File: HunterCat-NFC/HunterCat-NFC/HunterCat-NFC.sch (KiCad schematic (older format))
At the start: 66 parts, among them J1 Battery, J2 Conn_01x06_Female, P1 USB_C_Plug_USB2.0, Q1 DMG3415U-7, SW1 RESET, U1 ATSAMD21E18A, U2 PN7150B0HN_C11002E-PN7150B0HN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, U3 MCP73831-3-OT, U4 AP2112K-3.3, U5 GD25Q16CEIGR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

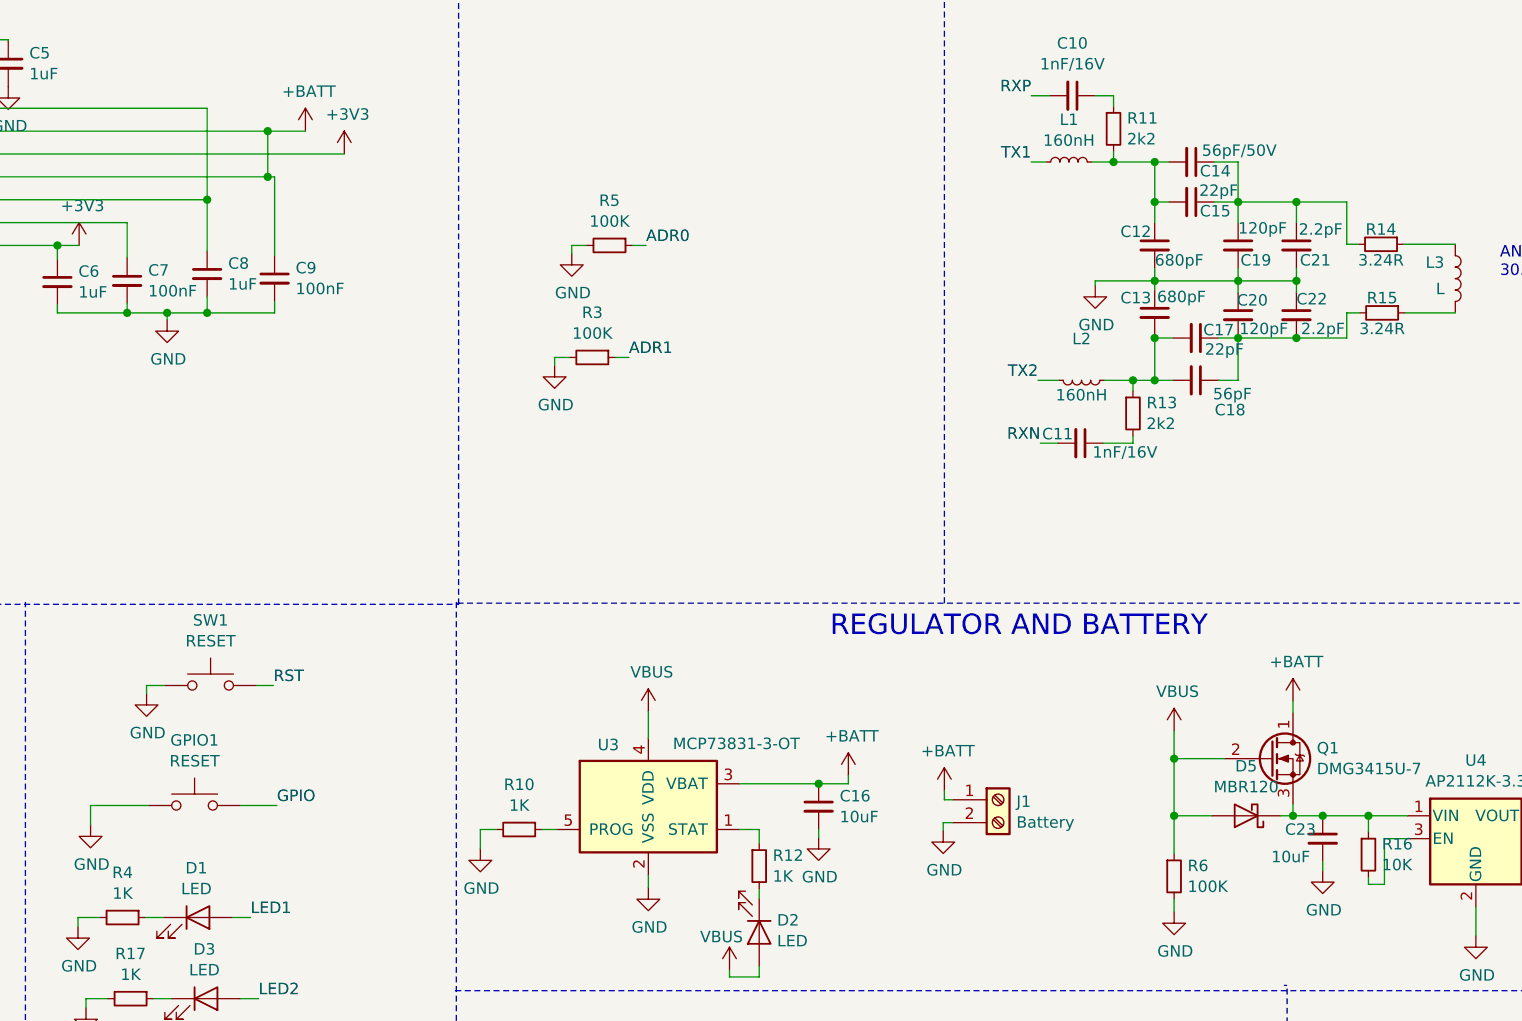
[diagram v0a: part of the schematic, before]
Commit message: modify Rf frontend
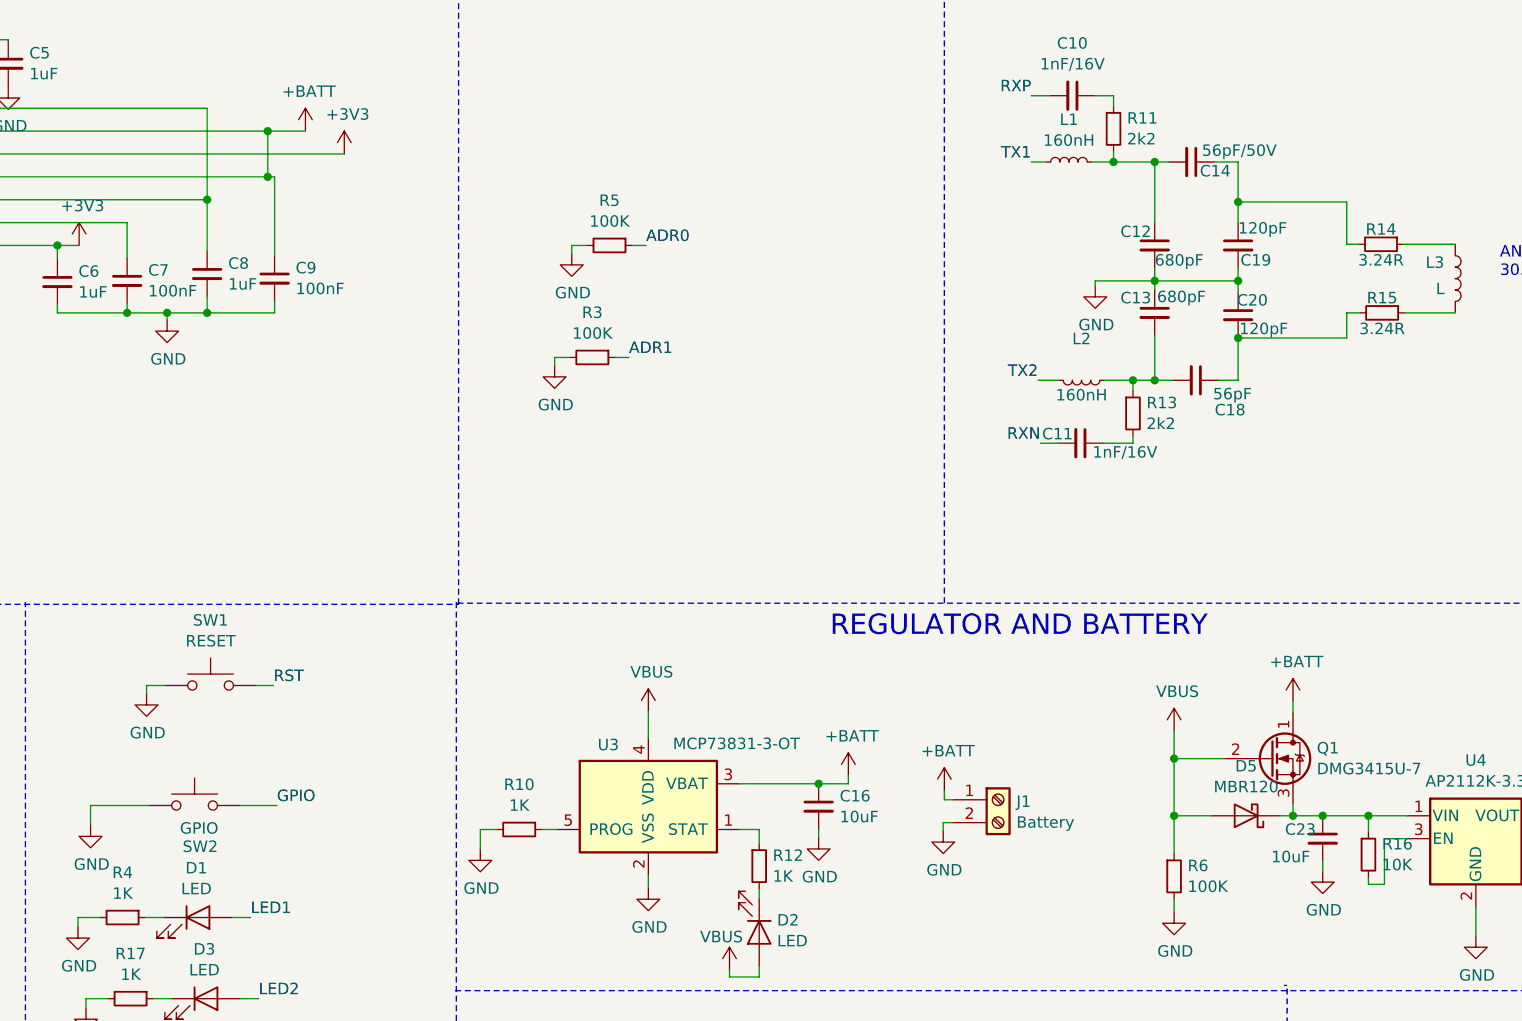
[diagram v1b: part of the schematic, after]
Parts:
- removed C15, C17: 22pF, Capacitor_SMD:C_0603_1608Metric_Pad1.05x0.95mm_HandSolder, symbol Device:C_Small
- removed C21, C22: 2.2pF, Capacitor_SMD:C_0603_1608Metric_Pad1.05x0.95mm_HandSolder, symbol Device:C_Small
- SW2: renamed from GPIO1; value RESET -> GPIO
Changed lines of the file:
@@
-$EndComp
-$Comp
-L Device:C_Small C15
-U 1 1 5E463B1E
-P 8930 1650
-F 0 "C15" V 8970 1755 50  0000 C CNN
-F 1 "22pF" V 8880 1770 50  0000 C CNN
-F 2 "Capacitor_SMD:C_0603_1608Metric_Pad1.05x0.95mm_HandSolder" H 8930 1650 50  0001 C CNN
-F 3 "~" H 8930 1650 50  0001 C CNN
-F 4 "06035A220JAT4A" H 8930 1650 50  0001 C CNN "manf#"
-	1    8930 1650
-	0    1    1    0
 $EndComp
 $Comp
@@
 $EndComp
 $Comp
-L Device:C_Small C21
-U 1 1 5E4643F2
-P 9390 1840
-F 0 "C21" H 9405 1775 50  0000 L CNN
-F 1 "2.2pF" H 9400 1910 50  0000 L CNN
-F 2 "Capacitor_SMD:C_0603_1608Metric_Pad1.05x0.95mm_HandSolder" H 9390 1840 50  0001 C CNN
-F 3 "~" H 9390 1840 50  0001 C CNN
-F 4 "GCM0335C1E2R2CA16D" H 9390 1840 50  0001 C CNN "manf#"
-	1    9390 1840
-	1    0    0    -1
-$EndComp
-$Comp
 L Device:C_Small C13
 U 1 1 5E464863
@@
 	1    9135 2145
 	1    0    0    -1
-$EndComp
-$Comp
-L Device:C_Small C22
-U 1 1 5E464CCF
-P 9390 2145
-F 0 "C22" H 9390 2215 50  0000 L CNN
-F 1 "2.2pF" H 9410 2085 50  0000 L CNN
-F 2 "Capacitor_SMD:C_0603_1608Metric_Pad1.05x0.95mm_HandSolder" H 9390 2145 50  0001 C CNN
-F 3 "~" H 9390 2145 50  0001 C CNN
-F 4 "GCM0335C1E2R2CA16D" H 9390 2145 50  0001 C CNN "manf#"
-	1    9390 2145
-	1    0    0    -1
-$EndComp
-$Comp
-L Device:C_Small C17
-U 1 1 5E4654A1
-P 8950 2245
-F 0 "C17" V 8915 2345 50  0000 C CNN
-F 1 "22pF" V 9000 2370 50  0000 C CNN
-F 2 "Capacitor_SMD:C_0603_1608Metric_Pad1.05x0.95mm_HandSolder" H 8950 2245 50  0001 C CNN
-F 3 "~" H 8950 2245 50  0001 C CNN
-F 4 "06035A220JAT4A" H 8950 2245 50  0001 C CNN "manf#"
-	1    8950 2245
-	0    1    1    0
 $EndComp
 $Comp
@@
 	8590 1475 8770 1475
 Connection ~ 8590 1475
-Wire Wire Line
-	8830 1650 8770 1650
-Wire Wire Line
-	8770 1650 8770 1475
 Connection ~ 8770 1475
 Wire Wire Line
@@
 	9030 1475 9135 1475
 Wire Wire Line
-	9135 1650 9030 1650
-Wire Wire Line
-	8770 1650 8770 1740
-Connection ~ 8770 1650
-Wire Wire Line
 	8770 1940 8770 1995
 Wire Wire Line
 	9135 2045 9135 1995
-Wire Wire Line
-	9390 1940 9390 1995
-Wire Wire Line
-	9390 1995 9135 1995
-Connection ~ 9390 1995
-Wire Wire Line
-	9390 1995 9390 2045
 Connection ~ 9135 1995
 Wire Wire Line
@@
 	8770 1995 8770 2035
 Wire Wire Line
-	9135 2245 9050 2245
-Wire Wire Line
-	8850 2245 8770 2245
-Wire Wire Line
-	8770 2245 8770 2235
-Wire Wire Line
 	9050 2430 9135 2430
 Wire Wire Line
@@
 	8850 2430 8770 2430
 Wire Wire Line
-	8770 2430 8770 2245
-Connection ~ 8770 2245
-Wire Wire Line
 	8770 2430 8675 2430
 Connection ~ 8770 2430
@@
 Wire Wire Line
 	8675 2705 8545 2705
-Wire Wire Line
-	9390 2245 9135 2245
 Wire Wire Line
 	8770 1995 8510 1995
@@
 Wire Wire Line
 	9610 2135 9610 2245
-Wire Wire Line
-	9610 2245 9390 2245
-Connection ~ 9390 2245
 Text Label 8230 1185 2    50   ~ 0
 RXP
@@
 $EndComp
 Wire Wire Line
-	9390 1740 9390 1650
-Wire Wire Line
-	9390 1650 9610 1650
-Wire Wire Line
 	9135 1475 9135 1650
-Wire Wire Line
-	9135 1650 9390 1650
 Connection ~ 9135 1650
 Wire Wire Line
 	9135 1650 9135 1740
-Connection ~ 9390 1650
 $Comp
 L Device:C_Small C25
@@
 	8505 5870 8505 5955
 $Comp
-L Switch:SW_Push GPIO1
+L Switch:SW_Push SW2
 U 1 1 5F214F20
 P 4570 4290
-F 0 "GPIO1" H 4570 4575 50  0000 C CNN
-F 1 "RESET" H 4570 4484 50  0000 C CNN
+F 0 "SW2" H 4595 4110 50  0000 C CNN
+F 1 "GPIO" H 4590 4190 50  0000 C CNN
 F 2 "Button_Switch_SMD:SW_SPST_TL3342" H 4570 4490 50  0001 C CNN
 F 3 "~" H 4570 4490 50  0001 C CNN
@@
 Wire Wire Line
 	3460 3140 3500 3140
+Wire Wire Line
+	8770 1475 8770 1740
+Wire Wire Line
+	8770 2235 8770 2430
+Wire Wire Line
+	9135 2245 9610 2245
+Wire Wire Line
+	9135 1650 9610 1650
 $EndSCHEMATC

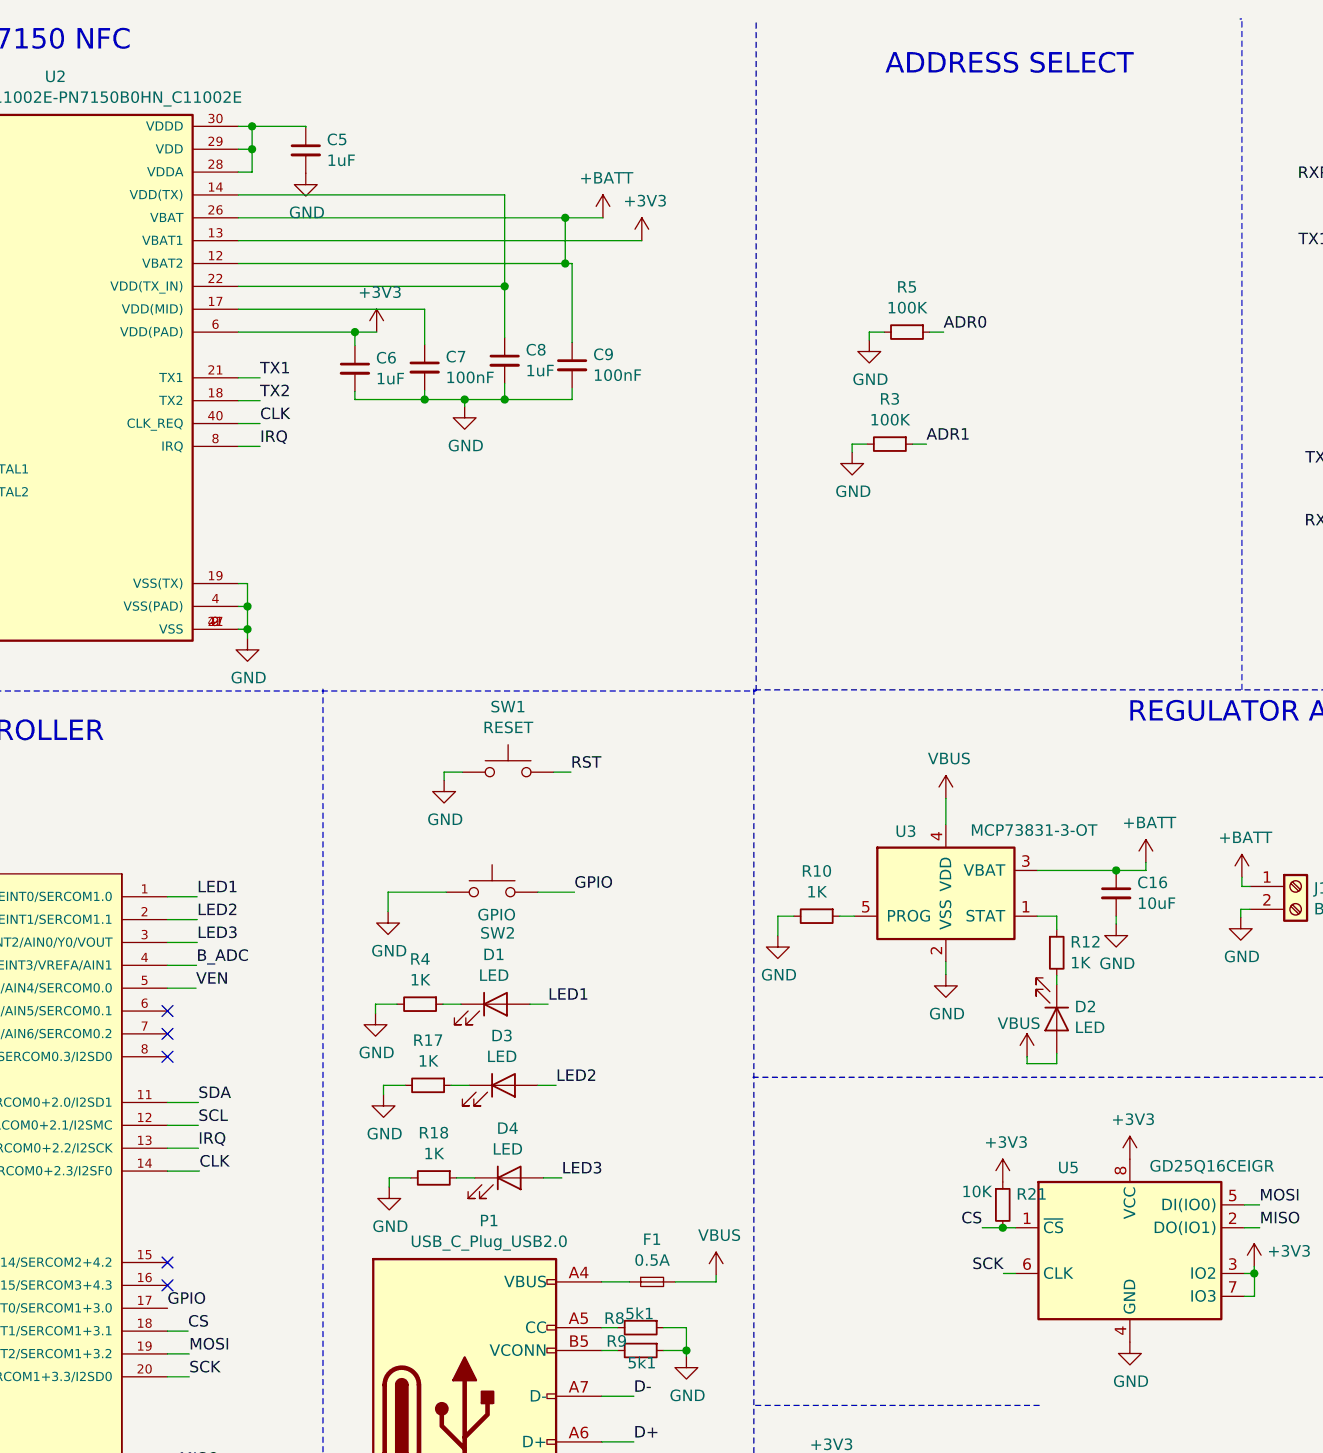
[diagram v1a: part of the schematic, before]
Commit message: Add button
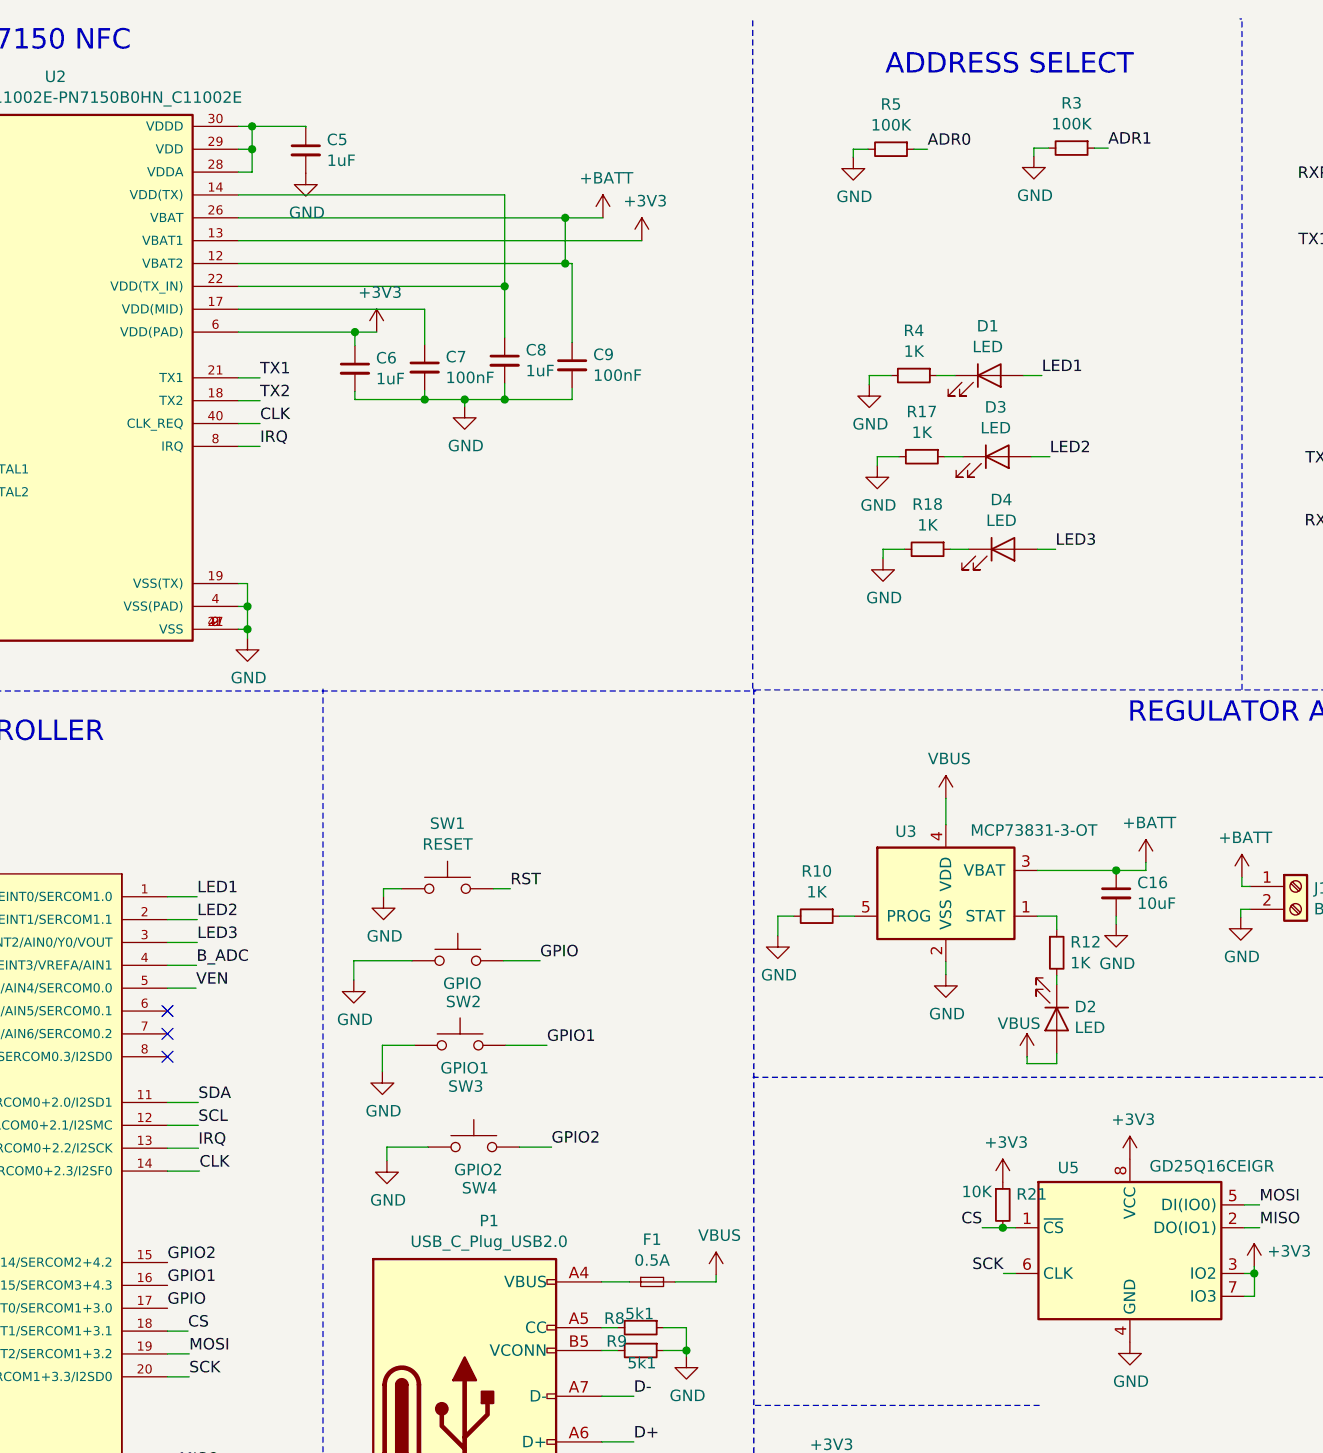
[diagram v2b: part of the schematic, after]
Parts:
- added SW3: GPIO1, Button_Switch_SMD:SW_SPST_TL3342, symbol Switch:SW_Push
- added SW4: GPIO2, Button_Switch_SMD:SW_SPST_TL3342, symbol Switch:SW_Push
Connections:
- net GND: now also SW3.1, SW4.1
- net GPIO2: now reaches U1.15 (PA14/EINT14/SERCOM2+4.2)
- net GPIO2: now also SW4.2
- net GPIO1: now reaches U1.16 (PA15/EINT15/SERCOM3+4.3)
- net GPIO1: now also SW3.2
- no-connect marks 10 -> 8
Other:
- moved on the sheet: D1, D3, D4, R17, R18, R3, R4, R5, SW1, SW2

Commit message: update to 1.0v
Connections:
- net CLK: now also U1.17 (PA16/I2C/EINT0/SERCOM1+3.0); no longer U1.14 (PA11/EINT11/AIN19/SERCOM0+2.3/I2SF0)
- net GPIO: now also SW4.2, U1.25 (PA27/EINT15); no longer SW2.2, U1.17 (PA16/I2C/EINT0/SERCOM1+3.0)
- net GPIO1: now also SW2.2, U1.14 (PA11/EINT11/AIN19/SERCOM0+2.3/I2SF0); no longer SW3.2, U1.16 (PA15/EINT15/SERCOM3+4.3)
- net GPIO2: now also SW3.2, U1.13 (PA10/EINT10/AIN18/SERCOM0+2.2/I2SCK); no longer SW4.2, U1.15 (PA14/EINT14/SERCOM2+4.2)
- net IRQ: now also U1.16 (PA15/EINT15/SERCOM3+4.3); no longer U1.13 (PA10/EINT10/AIN18/SERCOM0+2.2/I2SCK)
- net VEN: now also U1.15 (PA14/EINT14/SERCOM2+4.2); no longer U1.5 (PA04/EINT4/VREFB/AIN4/SERCOM0.0)
- no-connect marks 8 -> 7
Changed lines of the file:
@@
 Wire Wire Line
 	3150 5510 3290 5510
-Text Label 3285 5410 0    50   ~ 0
-IRQ
-Text Label 3290 5510 0    50   ~ 0
-CLK
 $Comp
 L Switch:SW_Push SW1
@@
 NoConn ~ 3150 5010
 NoConn ~ 3150 7310
-NoConn ~ 3150 7210
 NoConn ~ 3150 6910
 Text Notes 7350 3560 0    89   ~ 0
@@
 Wire Wire Line
 	3150 4710 3275 4710
-Text Label 3275 4710 0    50   ~ 0
+Text Label 3150 5910 0    50   ~ 0
 VEN
 Wire Wire Line
@@
 Wire Wire Line
 	8505 5870 8505 5955
-Text Label 3150 6110 0    50   ~ 0
+Text Label 3255 7210 0    50   ~ 0
 GPIO
 $Comp
@@
 Wire Wire Line
 	9135 1650 9610 1650
-Text Label 3150 5910 0    50   ~ 0
+Text Label 3285 5410 0    50   ~ 0
 GPIO2
-Text Label 3150 6010 0    50   ~ 0
+Text Label 3290 5510 0    50   ~ 0
 GPIO1
 Wire Wire Line
@@
 Wire Wire Line
 	4690 5405 4830 5405
-Text Label 4830 5405 0    50   ~ 0
+Text Label 4810 4960 0    50   ~ 0
 GPIO2
 $Comp
@@
 	1    0    0    -1
 $EndComp
-Text Label 4810 4960 0    50   ~ 0
+Text Label 4780 4590 0    50   ~ 0
 GPIO1
 $Comp
@@
 Wire Wire Line
 	4620 4590 4780 4590
-Text Label 4780 4590 0    50   ~ 0
+Text Label 4830 5405 0    50   ~ 0
 GPIO
 $Comp
@@
 Wire Notes Line
 	5710 3400 5710 470
+Text Label 3150 6110 0    50   ~ 0
+CLK
+Text Label 3150 6010 0    50   ~ 0
+IRQ
+Wire Wire Line
+	3255 7210 3150 7210
 $EndSCHEMATC

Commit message: Update labels VEN and IRQ
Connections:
- no-connect marks 7 -> 8
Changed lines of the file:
@@
 Wire Wire Line
 	9705 4635 9705 4605
-Wire Wire Line
-	3150 4710 3275 4710
 Text Label 3150 5910 0    50   ~ 0
 VEN
@@
 Wire Wire Line
 	3255 7210 3150 7210
+NoConn ~ 3150 4710
 $EndSCHEMATC
